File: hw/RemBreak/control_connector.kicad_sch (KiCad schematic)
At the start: 1 part, among them J5 Conn_02x06_Odd_Even

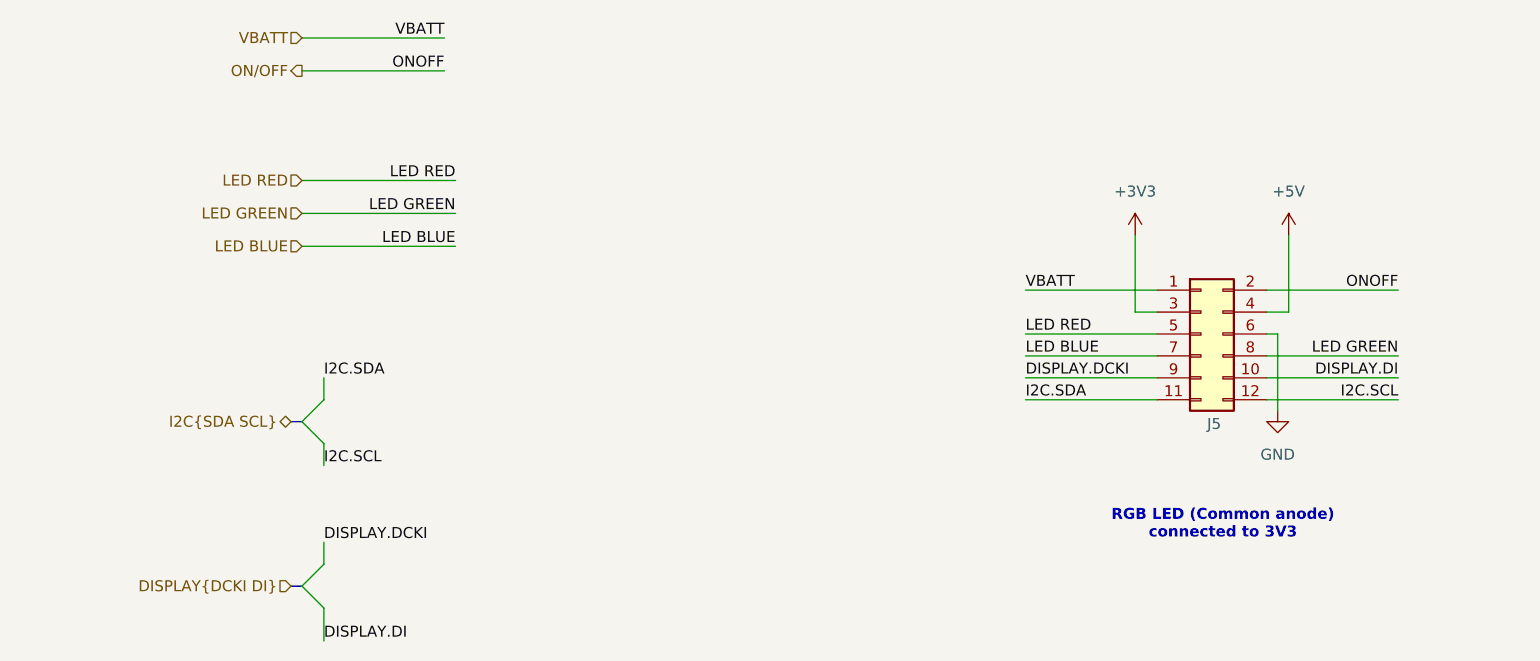
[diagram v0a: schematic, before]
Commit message: redrawing the schematics according the notes from the module design
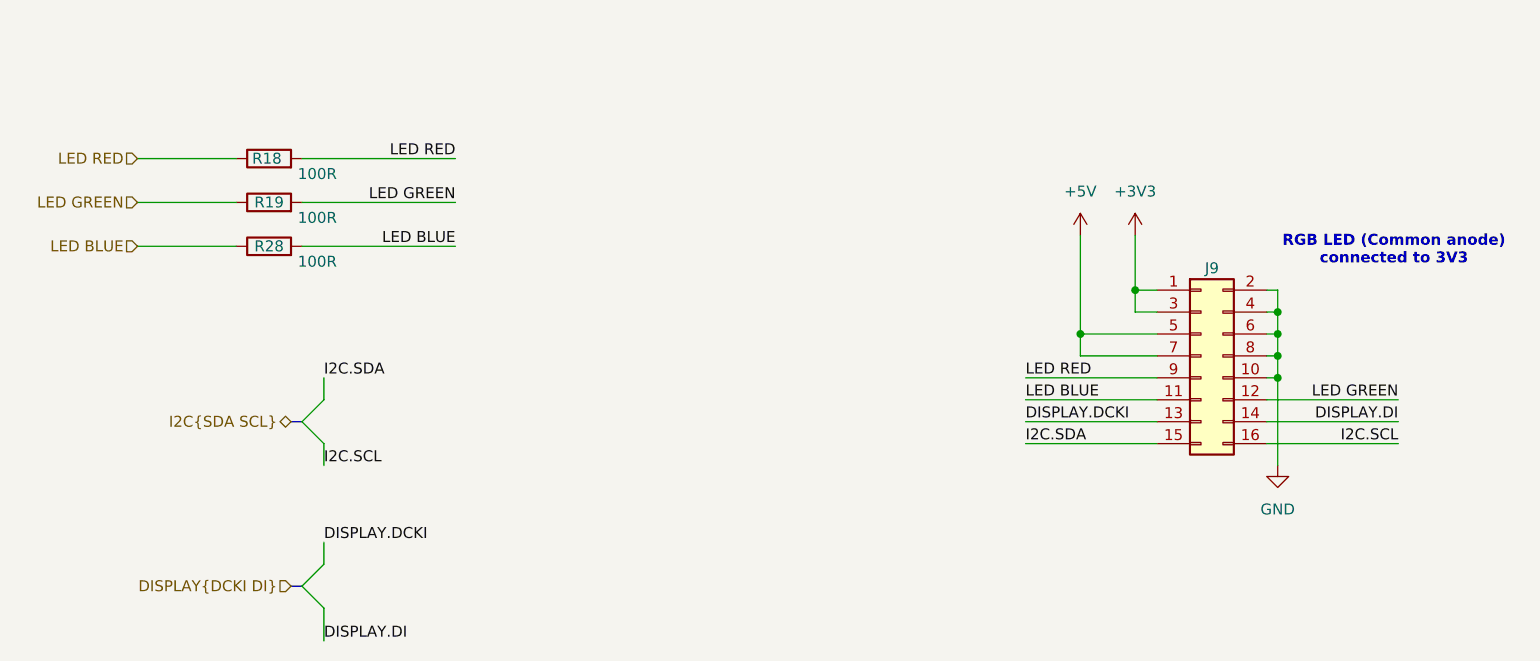
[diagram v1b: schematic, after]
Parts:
- removed J5: Conn_02x06_Odd_Even, chinese_modules:SAMTEC_TSM-106-01-L-DH-P-TR, symbol Connector_Generic:Conn_02x06_Odd_Even
- added J9: Conn_02x08_Odd_Even, dodo_conn:DF51K16DP2H800, symbol Connector_Generic:Conn_02x08_Odd_Even
- added R18, R19, R28: 100R, Resistor_SMD:R_0805_2012Metric_Pad1.20x1.40mm_HandSolder, symbol Device:R
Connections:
- net +3V3: now also J9.1 (Pin_1), J9.3 (Pin_3)
- net +5V: now also J9.5 (Pin_5), J9.7 (Pin_7)
- net DISPLAY.DCKI: now also J9.13 (Pin_13)
- net DISPLAY.DI: now also J9.14 (Pin_14)
- net GND: now also J9.10 (Pin_10), J9.2 (Pin_2), J9.4 (Pin_4), J9.6 (Pin_6), J9.8 (Pin_8)
- net I2C.SCL: now also J9.16 (Pin_16)
- net I2C.SDA: now also J9.15 (Pin_15)
- net LED BLUE: now also J9.11 (Pin_11), R28.1, R28.2
- net LED GREEN: now also J9.12 (Pin_12), R19.1, R19.2
- net LED RED: now also J9.9 (Pin_9), R18.1, R18.2
